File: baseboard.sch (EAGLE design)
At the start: 100 parts, among them IC1 LM321MF, J1 CONNECTOR-HEADER-2X2P2X2P-2.5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, J10 CONNECTOR-HEADER-2X2P2X2P-2.5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, J11 CONNECTOR-HEADER-2X2P2X2P-2.5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, J12 CONNECTOR-HEADER-2X2P2X2P-2.5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, J13 CONNECTOR-HEADER-2X2P2X2P-2.5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, J14 CONNECTOR-HEADER-2X2P2X2P-2.5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, J15 CONNECTOR-HEADER-2X2P2X2P-2.5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, J16 CONNECTOR-HEADER-2X2P2X2P-2.5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, J17 CONNECTOR-HEADER-2X2P2X2P-2.5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, J18 CONNECTOR-HEADER-2X2P2X2P-2.5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, J19 CONNECTOR-HEADER-2X2P2X2P-2.5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, J2 CONNECTOR-HEADER-2X2P2X2P-2.5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, J20 CONNECTOR-HEADER-2X2P2X2P-2.5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, J21 CONNECTOR-HEADER-2X2P2X2P-2.5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, J22 CONNECTOR-HEADER-2X2P2X2P-2.5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, J23 CONNECTOR-HEADER-2X2P2X2P-2.5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, J24 CONNECTOR-HEADER-2X2P2X2P-2.5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, J25 CONNECTOR-HEADER-2X2P2X2P-2.5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, J26 CONNECTOR-HEADER-2X2P2X2P-2.5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, J27 CONNECTOR-HEADER-2X2P2X2P-2.5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, J28 CONNECTOR-HEADER-2X2P2X2P-2.5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, J29 CONNECTOR-HEADER-2X2P2X2P-2.5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, J3 CONNECTOR-HEADER-2X2P2X2P-2.5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, J30 CONNECTOR-HEADER-2X2P2X2P-2.5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, J31 CONNECTOR-HEADER-2X2P2X2P-2.5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, J32 CONNECTOR-HEADER-2X2P2X2P-2.5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, J33 CONNECTOR-HEADER-2X2P2X2P-2.5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, J34 CONNECTOR-HEADER-2X2P2X2P-2.5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, J35 CONNECTOR-HEADER-2X2P2X2P-2.5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, J36 CONNECTOR-HEADER-2X2P2X2P-2.5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, J37 CONNECTOR-HEADER-2X2P2X2P-2.5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, J38 CONNECTOR-HEADER-2X2P2X2P-2.5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, J39 CONNECTOR-HEADER-2X2P2X2P-2.5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, J4 CONNECTOR-HEADER-2X2P2X2P-2.5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, J40 CONNECTOR-HEADER-2X2P2X2P-2.5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, J41 CONNECTOR-HEADER-2X2P2X2P-2.5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, J42 CONNECTOR-HEADER-2X2P2X2P-2.5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, J43 CONNECTOR-HEADER-2X2P2X2P-2.5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, J44 CONNECTOR-HEADER-2X2P2X2P-2.5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, J45 CONNECTOR-HEADER-2X2P2X2P-2.5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, J46 CONNECTOR-HEADER-2X2P2X2P-2.5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, J47 CONNECTOR-HEADER-2X2P2X2P-2.5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, J48 CONNECTOR-HEADER-2X2P2X2P-2.5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, J49 CONNECTOR-HEADER-2X2P2X2P-2.5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, J5 CONNECTOR-HEADER-2X2P2X2P-2.5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, J50 CONNECTOR-HEADER-2X2P2X2P-2.5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, J51 CONNECTOR-HEADER-2X2P2X2P-2.5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, J52 CONNECTOR-HEADER-2X2P2X2P-2.5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, J53 CONNECTOR-HEADER-2X2P2X2P-2.5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, J54 CONNECTOR-HEADER-2X2P2X2P-2.5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, J55 CONNECTOR-HEADER-2X2P2X2P-2.5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, J56 CONNECTOR-HEADER-2X2P2X2P-2.5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, J57 CONNECTOR-HEADER-2X2P2X2P-2.5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, J58 CONNECTOR-HEADER-2X2P2X2P-2.5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, J59 CONNECTOR-HEADER-2X2P2X2P-2.5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, J6 CONNECTOR-HEADER-2X2P2X2P-2.5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, J60 CONNECTOR-HEADER-2X2P2X2P-2.5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, J61 CONNECTOR-HEADER-2X2P2X2P-2.5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, J62 CONNECTOR-HEADER-2X2P2X2P-2.5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, J63 CONNECTOR-HEADER-2X2P2X2P-2.5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, J64 CONNECTOR-HEADER-2X2P2X2P-2.5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, J7 CONNECTOR-HEADER-2X2P2X2P-2.5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, J8 CONNECTOR-HEADER-2X2P2X2P-2.5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, J9 CONNECTOR-HEADER-2X2P2X2P-2.5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, Q3 MOSFET-N-044020001, U2 ADXL335

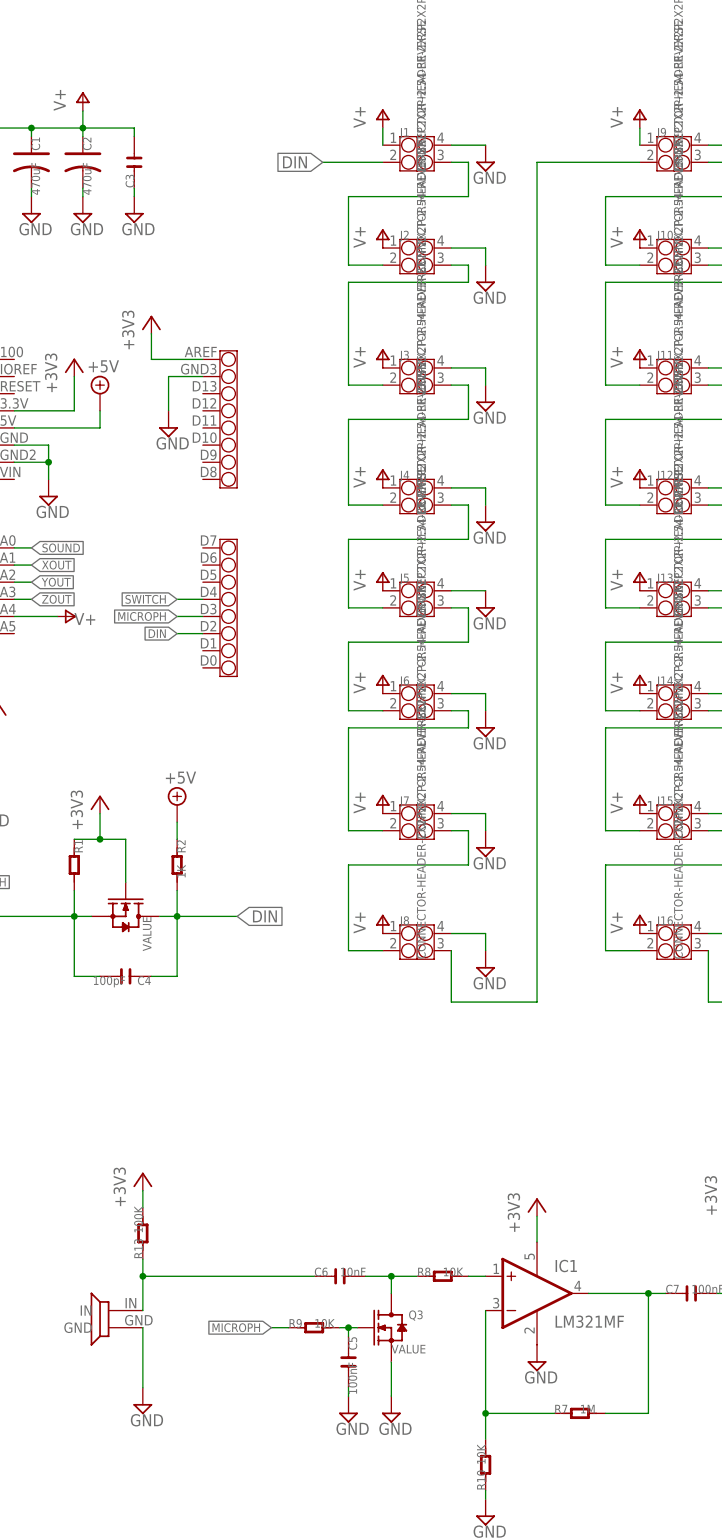
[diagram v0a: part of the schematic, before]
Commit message: added LED sticks and acrylic case files
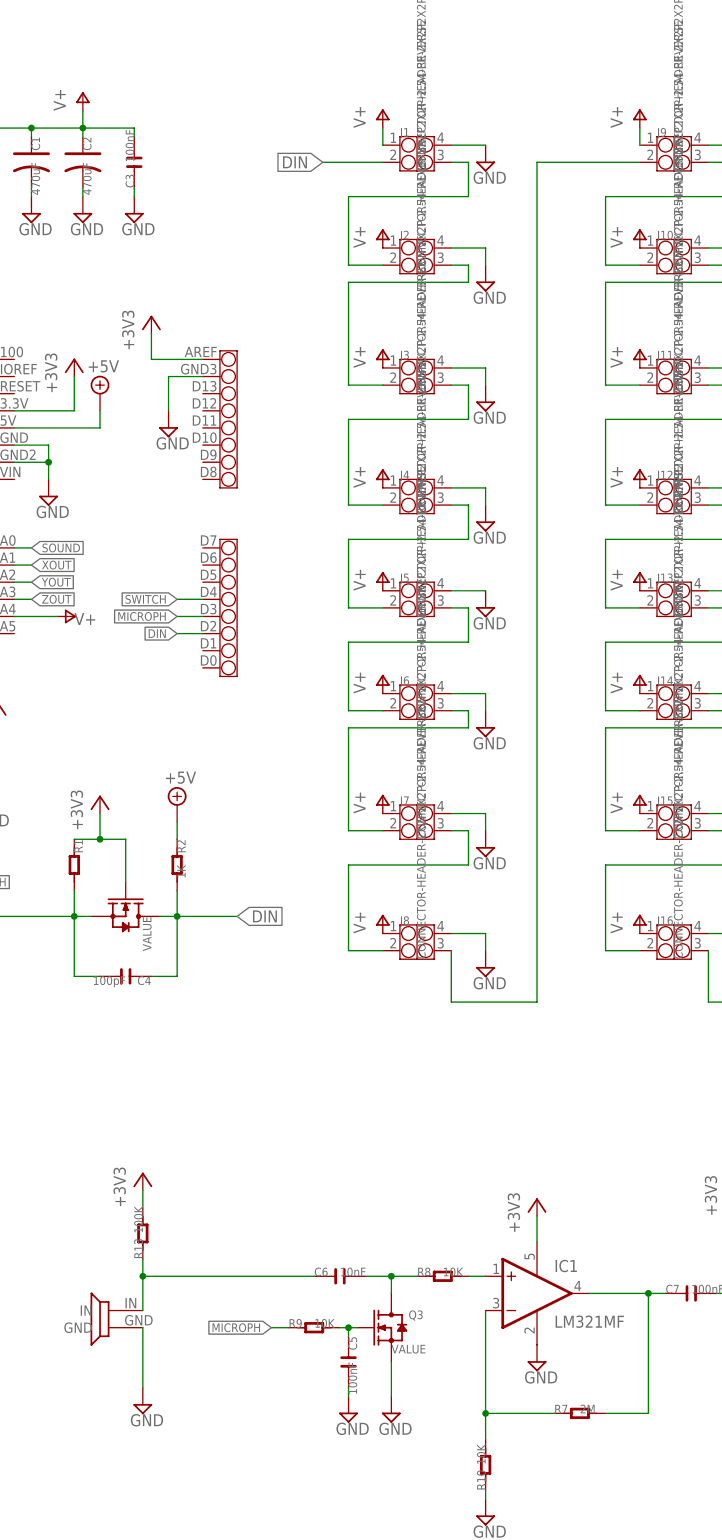
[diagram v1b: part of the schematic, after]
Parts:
- C3: value (none) -> 100nF
- R7: value 1M -> 2M
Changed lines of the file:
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@@
 <setting verticaltext="up"/>
 </settings>
-<grid distance="50" unitdist="mil" unit="mil" style="lines" multiple="1" display="yes" altdistance="0.01" altunitdist="inch" altunit="inch"/>
+<grid distance="0.1" unitdist="inch" unit="inch" style="lines" multiple="1" display="no" altdistance="0.01" altunitdist="inch" altunit="inch"/>
 <layers>
 <layer number="1" name="Top" color="4" fill="1" visible="no" active="no"/>
@@
 <part name="SV1" library="con-amp-mt" deviceset="S04P" device=""/>
 <part name="A1" library="OPL Eagle Library" deviceset="ARDUINOSHIELD" device=""/>
-<part name="C3" library="OPL Eagle Library" deviceset="C*" device="-0603"/>
+<part name="C3" library="OPL Eagle Library" deviceset="C*" device="-0603" value="100nF"/>
 <part name="J1" library="OPL Eagle Library" deviceset="CONNECTOR-HEADER-2X2P" device="2X2P-2.54-REVERSE" value="CONNECTOR-HEADER-2X2P2X2P-2.54-REVERSE"/>
 <part name="J2" library="OPL Eagle Library" deviceset="CONNECTOR-HEADER-2X2P" device="2X2P-2.54-REVERSE" value="CONNECTOR-HEADER-2X2P2X2P-2.54-REVERSE"/>
@@
 <part name="C4" library="OPL Eagle Library" deviceset="C*" device="-0603" value="100pF"/>
 <part name="IC1" library="linear" deviceset="LM321?*" device="MF"/>
-<part name="R7" library="OPL Eagle Library" deviceset="R*" device="-0603" value="1M"/>
+<part name="R7" library="OPL Eagle Library" deviceset="R*" device="-0603" value="2M"/>
 <part name="R8" library="OPL Eagle Library" deviceset="R*" device="-0603" value="10K"/>
 <part name="R9" library="OPL Eagle Library" deviceset="R*" device="-0603" value="10K"/>
